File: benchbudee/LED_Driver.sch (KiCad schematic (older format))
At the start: 0 parts

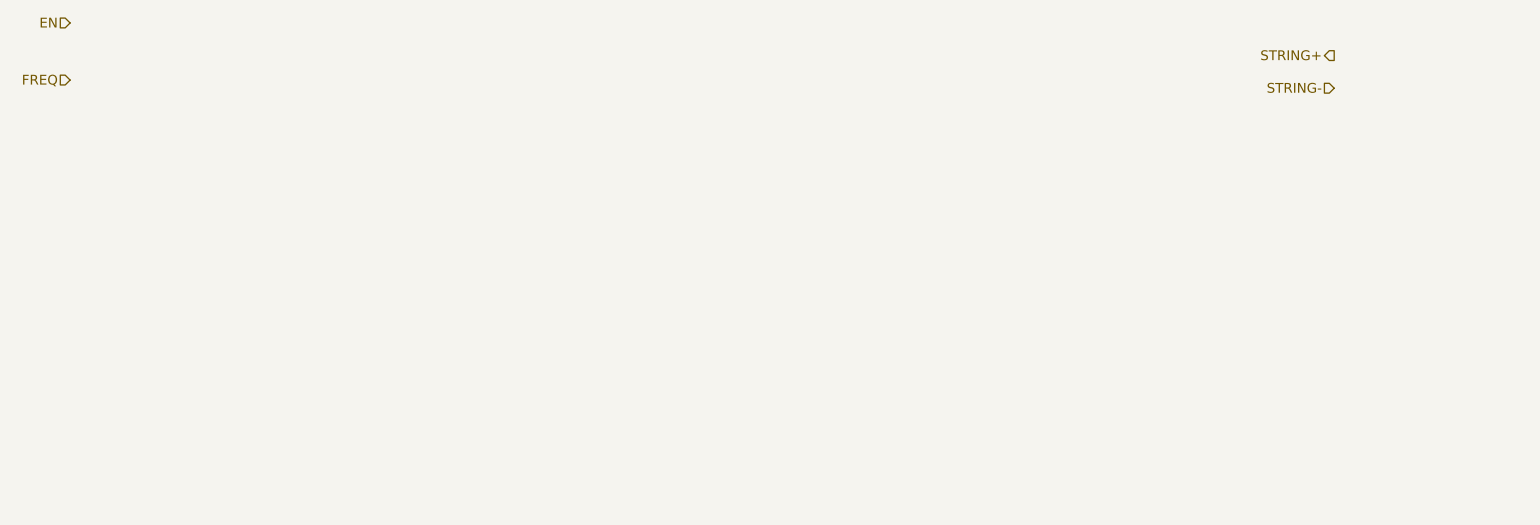
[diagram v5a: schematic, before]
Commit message: Added LED driver.
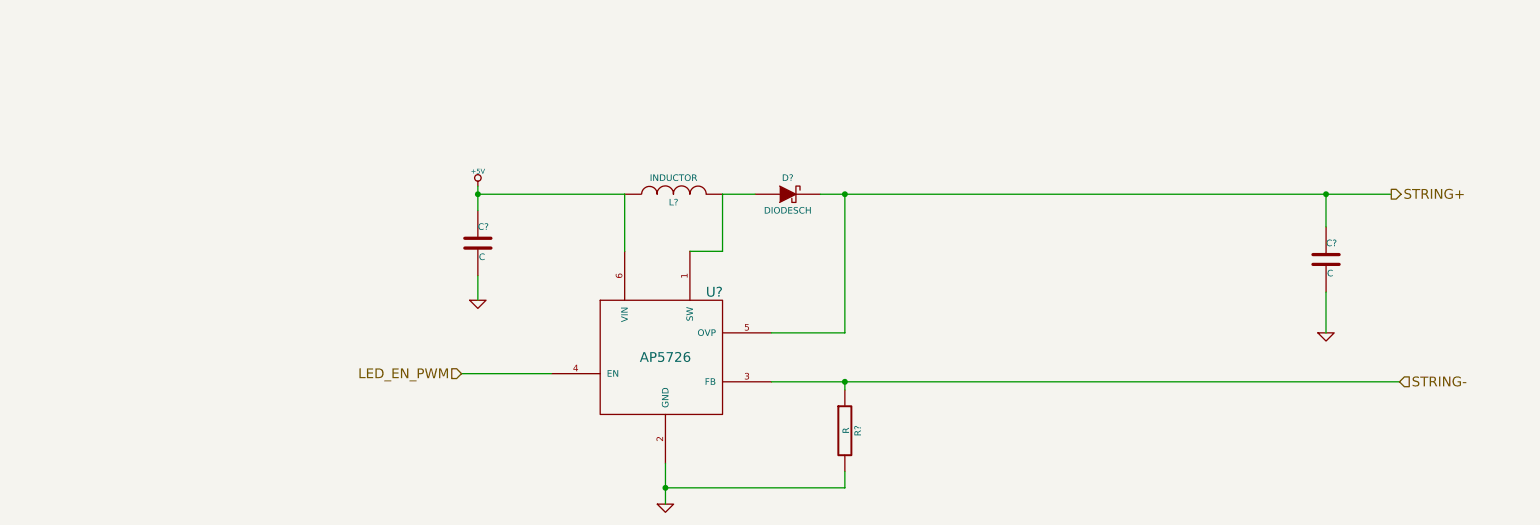
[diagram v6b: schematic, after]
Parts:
- added C? (x2): C, ~, symbol C
- added D?: DIODESCH, ~, symbol DIODESCH
- added L?: INDUCTOR, ~, symbol INDUCTOR
- added R?: R, ~, symbol R
- added U?: AP5726, symbol AP5726
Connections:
- net STRING+: now also C?.1, D?.2 (K), U?.5 (OVP)
- net STRING-: now also R?.1, U?.3 (FB)
- new net: D?.1 (A), L?.2, U?.1 (SW)
- new net +5V: C?.1, L?.1, U?.6 (VIN)
- new net GND: C?.2, C?.2, R?.2, U?.2 (GND)
- new net LED_EN_PWM: U?.4 (EN)
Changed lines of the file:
@@
 Comment4 ""
 $EndDescr
-Text HLabel 1000 1150 0    60   Input ~ 0
-EN
-Text HLabel 1000 1500 0    60   Input ~ 0
-FREQ
-Text HLabel 8750 1350 0    60   Output ~ 0
+Text HLabel 3400 3300 0    60   Input ~ 0
+LED_EN_PWM
+Text HLabel 9100 2200 2    60   Output ~ 0
 STRING+
-Text HLabel 8750 1550 0    60   Input ~ 0
+Text HLabel 9150 3350 2    60   Input ~ 0
 STRING-
+$Comp
+L AP5726 U?
+U 1 1 52FF56C0
+P 4650 3200
+F 0 "U?" H 4950 3600 60  0000 C CNN
+F 1 "AP5726" H 4650 3200 60  0000 C CNN
+F 2 "" H 4250 3300 60  0000 C CNN
+F 3 "" H 4250 3300 60  0000 C CNN
+	1    4650 3200
+	1    0    0    -1
+$EndComp
+Wire Wire Line
+	3400 3300 3950 3300
+$Comp
+L +5V #PWR?
+U 1 1 52FF5DB5
+P 3500 2150
+F 0 "#PWR?" H 3500 2240 20  0001 C CNN
+F 1 "+5V" H 3500 2240 30  0000 C CNN
+F 2 "" H 3500 2150 60  0000 C CNN
+F 3 "" H 3500 2150 60  0000 C CNN
+	1    3500 2150
+	1    0    0    -1
+$EndComp
+$Comp
+L GND #PWR?
+U 1 1 52FF5DCE
+P 3500 2850
+F 0 "#PWR?" H 3500 2850 30  0001 C CNN
+F 1 "GND" H 3500 2780 30  0001 C CNN
+F 2 "" H 3500 2850 60  0000 C CNN
+F 3 "" H 3500 2850 60  0000 C CNN
+	1    3500 2850
+	1    0    0    -1
+$EndComp
+$Comp
+L C C?
+U 1 1 52FF5DF1
+P 3500 2500
+F 0 "C?" H 3500 2600 40  0000 L CNN
+F 1 "C" H 3506 2415 40  0000 L CNN
+F 2 "~" H 3538 2350 30  0000 C CNN
+F 3 "~" H 3500 2500 60  0000 C CNN
+	1    3500 2500
+	1    0    0    -1
+$EndComp
+Wire Wire Line
+	3500 2150 3500 2200
+Wire Wire Line
+	3500 2200 3500 2300
+Wire Wire Line
+	3500 2200 4400 2200
+Wire Wire Line
+	4400 2200 4400 2550
+Connection ~ 3500 2200
+Wire Wire Line
+	3500 2700 3500 2850
+$Comp
+L INDUCTOR L?
+U 1 1 52FF5E1F
+P 4700 2200
+F 0 "L?" V 4650 2200 40  0000 C CNN
+F 1 "INDUCTOR" V 4800 2200 40  0000 C CNN
+F 2 "~" H 4700 2200 60  0000 C CNN
+F 3 "~" H 4700 2200 60  0000 C CNN
+	1    4700 2200
+	0    -1   -1   0
+$EndComp
+Wire Wire Line
+	4800 2550 4800 2550
+Wire Wire Line
+	4800 2550 5000 2550
+Wire Wire Line
+	5000 2200 5200 2200
+$Comp
+L DIODESCH D?
+U 1 1 52FF5E46
+P 5400 2200
+F 0 "D?" H 5400 2300 40  0000 C CNN
+F 1 "DIODESCH" H 5400 2100 40  0000 C CNN
+F 2 "~" H 5400 2200 60  0000 C CNN
+F 3 "~" H 5400 2200 60  0000 C CNN
+	1    5400 2200
+	1    0    0    -1
+$EndComp
+Wire Wire Line
+	5600 2200 5750 2200
+Wire Wire Line
+	5750 2200 8700 2200
+Wire Wire Line
+	8700 2200 9100 2200
+Wire Wire Line
+	8700 2200 8700 2400
+$Comp
+L C C?
+U 1 1 52FF5E7B
+P 8700 2600
+F 0 "C?" H 8700 2700 40  0000 L CNN
+F 1 "C" H 8706 2515 40  0000 L CNN
+F 2 "~" H 8738 2450 30  0000 C CNN
+F 3 "~" H 8700 2600 60  0000 C CNN
+	1    8700 2600
+	1    0    0    -1
+$EndComp
+$Comp
+L GND #PWR?
+U 1 1 52FF5E88
+P 4650 4100
+F 0 "#PWR?" H 4650 4100 30  0001 C CNN
+F 1 "GND" H 4650 4030 30  0001 C CNN
+F 2 "" H 4650 4100 60  0000 C CNN
+F 3 "" H 4650 4100 60  0000 C CNN
+	1    4650 4100
+	1    0    0    -1
+$EndComp
+$Comp
+L GND #PWR?
+U 1 1 52FF5E8E
+P 8700 3050
+F 0 "#PWR?" H 8700 3050 30  0001 C CNN
+F 1 "GND" H 8700 2980 30  0001 C CNN
+F 2 "" H 8700 3050 60  0000 C CNN
+F 3 "" H 8700 3050 60  0000 C CNN
+	1    8700 3050
+	1    0    0    -1
+$EndComp
+Wire Wire Line
+	8700 2800 8700 3050
+Wire Wire Line
+	4650 3850 4650 4000
+Wire Wire Line
+	4650 4000 4650 4100
+Wire Wire Line
+	5750 2200 5750 3050
+Wire Wire Line
+	5750 3050 5300 3050
+Connection ~ 5750 2200
+$Comp
+L R R?
+U 1 1 52FF5EC9
+P 5750 3650
+F 0 "R?" V 5830 3650 40  0000 C CNN
+F 1 "R" V 5757 3651 40  0000 C CNN
+F 2 "~" V 5680 3650 30  0000 C CNN
+F 3 "~" H 5750 3650 30  0000 C CNN
+	1    5750 3650
+	1    0    0    -1
+$EndComp
+Wire Wire Line
+	5750 3900 5750 4000
+Wire Wire Line
+	5750 4000 4650 4000
+Connection ~ 4650 4000
+Wire Wire Line
+	5300 3350 5750 3350
+Wire Wire Line
+	5750 3350 9150 3350
+Wire Wire Line
+	5750 3350 5750 3400
+Connection ~ 5750 3350
+Connection ~ 8700 2200
+Wire Wire Line
+	5000 2550 5000 2200
 $EndSCHEMATC

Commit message: Setting up for layout
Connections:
- net STRING+ renamed LED_STRING+
- net STRING- renamed LED_STRING-
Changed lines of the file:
@@
 LIBS:benchbudee-custom
 LIBS:benchbudee-cache
-EELAYER 27 0
+EELAYER 24 0
 EELAYER END
 $Descr A4 11693 8268
 encoding utf-8
-Sheet 6 9
+Sheet 5 9
 Title ""
 Date "14 feb 2014"
@@
 LED_EN_PWM
 Text HLabel 9100 2200 2    60   Output ~ 0
-STRING+
-Text HLabel 9150 3350 2    60   Input ~ 0
-STRING-
+LED_STRING+
+Text HLabel 9150 3350 2    60   Output ~ 0
+LED_STRING-
 $Comp
 L AP5726 U?

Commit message: Relay module footprints done
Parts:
- gave numbers to parts that had none: 6
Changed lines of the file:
@@
 LED_STRING-
 $Comp
-L AP5726 U?
+L AP5726 U5
 U 1 1 52FF56C0
 P 4650 3200
-F 0 "U?" H 4950 3600 60  0000 C CNN
+F 0 "U5" H 4950 3600 60  0000 C CNN
 F 1 "AP5726" H 4650 3200 60  0000 C CNN
 F 2 "" H 4250 3300 60  0000 C CNN
@@
 	3400 3300 3950 3300
 $Comp
-L +5V #PWR?
+L +5V #PWR027
 U 1 1 52FF5DB5
 P 3500 2150
-F 0 "#PWR?" H 3500 2240 20  0001 C CNN
+F 0 "#PWR027" H 3500 2240 20  0001 C CNN
 F 1 "+5V" H 3500 2240 30  0000 C CNN
 F 2 "" H 3500 2150 60  0000 C CNN
@@
 $EndComp
 $Comp
-L GND #PWR?
+L GND #PWR028
 U 1 1 52FF5DCE
 P 3500 2850
-F 0 "#PWR?" H 3500 2850 30  0001 C CNN
+F 0 "#PWR028" H 3500 2850 30  0001 C CNN
 F 1 "GND" H 3500 2780 30  0001 C CNN
 F 2 "" H 3500 2850 60  0000 C CNN
@@
 $EndComp
 $Comp
-L C C?
+L C C4
 U 1 1 52FF5DF1
 P 3500 2500
-F 0 "C?" H 3500 2600 40  0000 L CNN
+F 0 "C4" H 3500 2600 40  0000 L CNN
 F 1 "C" H 3506 2415 40  0000 L CNN
 F 2 "~" H 3538 2350 30  0000 C CNN
@@
 $EndComp
 Wire Wire Line
-	3500 2150 3500 2200
-Wire Wire Line
-	3500 2200 3500 2300
+	3500 2150 3500 2300
 Wire Wire Line
 	3500 2200 4400 2200
@@
 	3500 2700 3500 2850
 $Comp
-L INDUCTOR L?
+L INDUCTOR L4
 U 1 1 52FF5E1F
 P 4700 2200
-F 0 "L?" V 4650 2200 40  0000 C CNN
+F 0 "L4" V 4650 2200 40  0000 C CNN
 F 1 "INDUCTOR" V 4800 2200 40  0000 C CNN
 F 2 "~" H 4700 2200 60  0000 C CNN
@@
 $EndComp
 Wire Wire Line
-	4800 2550 4800 2550
-Wire Wire Line
 	4800 2550 5000 2550
 Wire Wire Line
 	5000 2200 5200 2200
 $Comp
-L DIODESCH D?
+L DIODESCH D4
 U 1 1 52FF5E46
 P 5400 2200
-F 0 "D?" H 5400 2300 40  0000 C CNN
+F 0 "D4" H 5400 2300 40  0000 C CNN
 F 1 "DIODESCH" H 5400 2100 40  0000 C CNN
 F 2 "~" H 5400 2200 60  0000 C CNN
@@
 $EndComp
 Wire Wire Line
-	5600 2200 5750 2200
-Wire Wire Line
-	5750 2200 8700 2200
-Wire Wire Line
-	8700 2200 9100 2200
+	5600 2200 9100 2200
 Wire Wire Line
 	8700 2200 8700 2400
 $Comp
-L C C?
+L C C5
 U 1 1 52FF5E7B
 P 8700 2600
-F 0 "C?" H 8700 2700 40  0000 L CNN
+F 0 "C5" H 8700 2700 40  0000 L CNN
 F 1 "C" H 8706 2515 40  0000 L CNN
 F 2 "~" H 8738 2450 30  0000 C CNN
@@
 $EndComp
 $Comp
-L GND #PWR?
+L GND #PWR029
 U 1 1 52FF5E88
 P 4650 4100
-F 0 "#PWR?" H 4650 4100 30  0001 C CNN
+F 0 "#PWR029" H 4650 4100 30  0001 C CNN
 F 1 "GND" H 4650 4030 30  0001 C CNN
 F 2 "" H 4650 4100 60  0000 C CNN
@@
 $EndComp
 $Comp
-L GND #PWR?
+L GND #PWR030
 U 1 1 52FF5E8E
 P 8700 3050
-F 0 "#PWR?" H 8700 3050 30  0001 C CNN
+F 0 "#PWR030" H 8700 3050 30  0001 C CNN
 F 1 "GND" H 8700 2980 30  0001 C CNN
 F 2 "" H 8700 3050 60  0000 C CNN
@@
 	8700 2800 8700 3050
 Wire Wire Line
-	4650 3850 4650 4000
-Wire Wire Line
-	4650 4000 4650 4100
+	4650 3850 4650 4100
 Wire Wire Line
 	5750 2200 5750 3050
@@
 Connection ~ 5750 2200
 $Comp
-L R R?
+L R R14
 U 1 1 52FF5EC9
 P 5750 3650
-F 0 "R?" V 5830 3650 40  0000 C CNN
+F 0 "R14" V 5830 3650 40  0000 C CNN
 F 1 "R" V 5757 3651 40  0000 C CNN
 F 2 "~" V 5680 3650 30  0000 C CNN
@@
 Connection ~ 4650 4000
 Wire Wire Line
-	5300 3350 5750 3350
-Wire Wire Line
-	5750 3350 9150 3350
+	5300 3350 9150 3350
 Wire Wire Line
 	5750 3350 5750 3400
